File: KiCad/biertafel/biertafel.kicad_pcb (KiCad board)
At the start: 2 copper layers, 39 parts, among them J1 Screw_Terminal_01x02, J10 Screw_Terminal_01x02, J11 Raspberry connectors, J12 Screw_Terminal_01x02, J13 Raspberry connectors, J14 VCC socket, J2 Screw_Terminal_01x02, J3 Screw_Terminal_01x02, J4 Screw_Terminal_01x02, J5 Screw_Terminal_01x02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

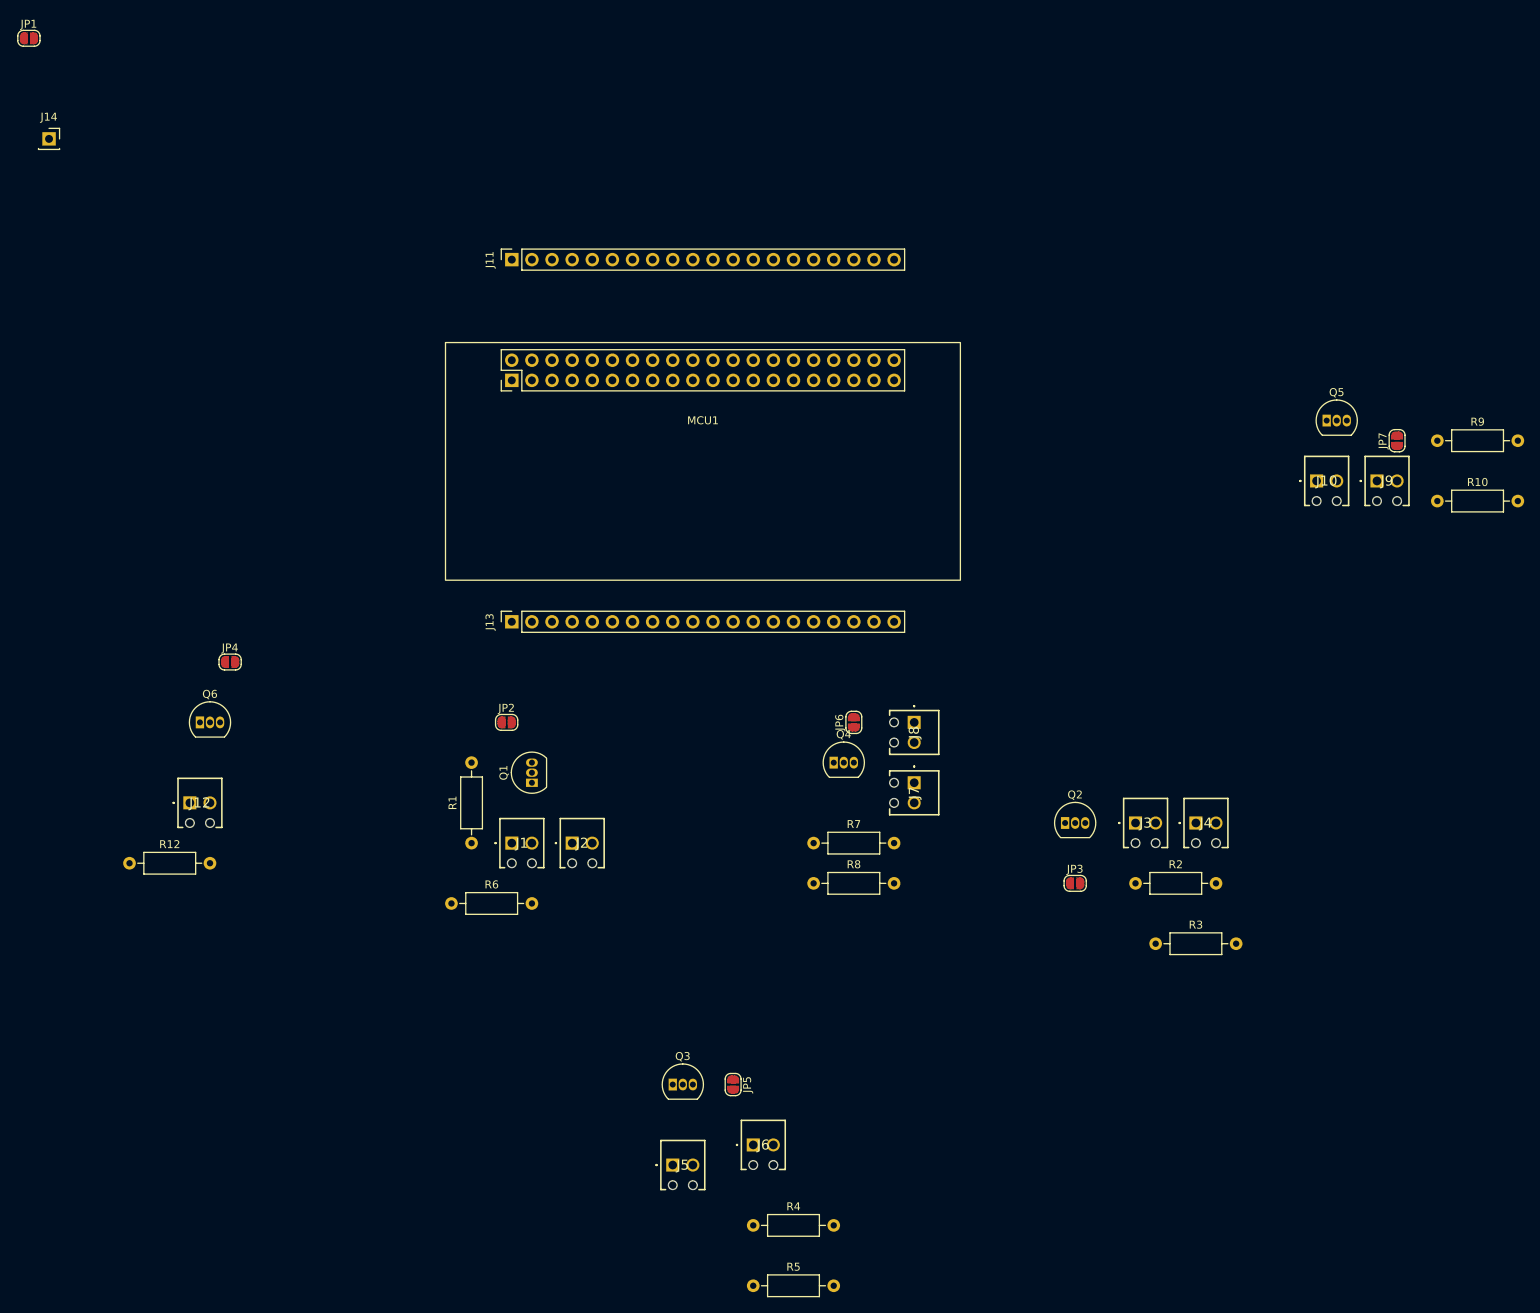
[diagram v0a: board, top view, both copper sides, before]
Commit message: In PCB layout, placed the objects to aprox position
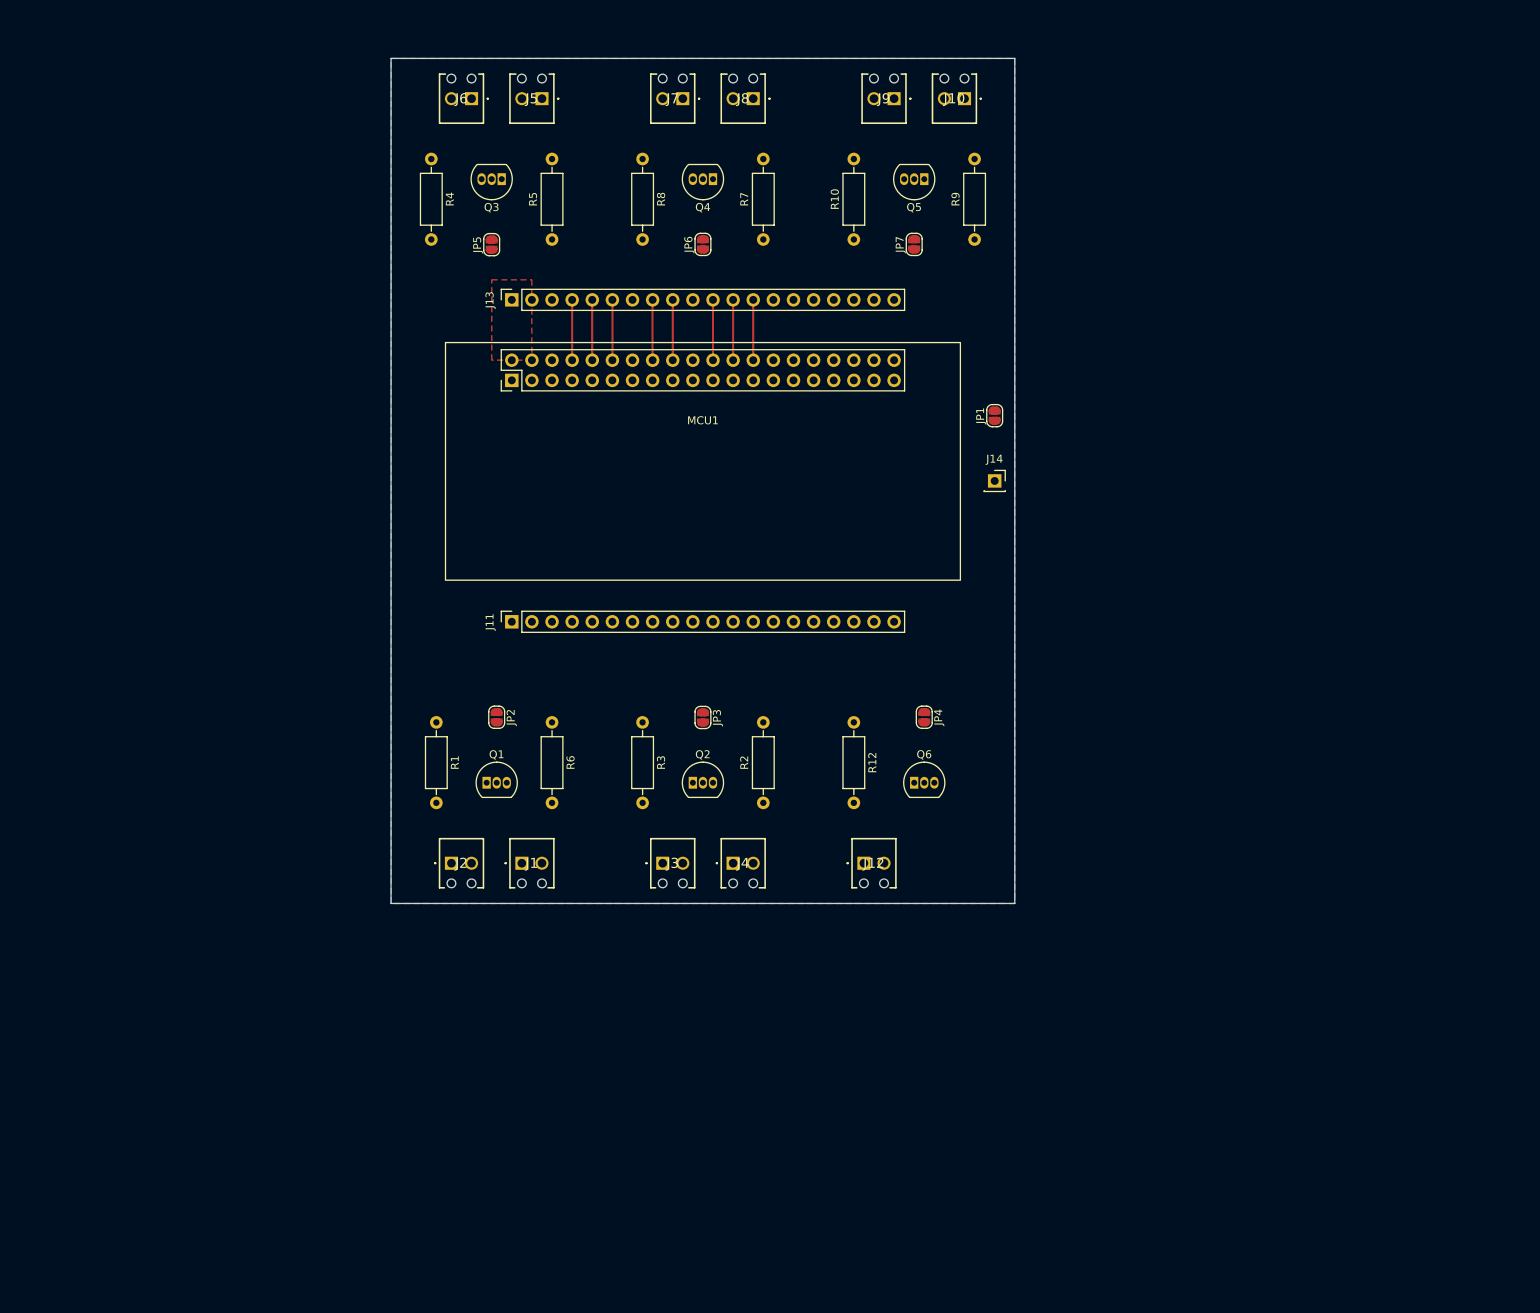
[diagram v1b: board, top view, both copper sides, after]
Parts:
- moved R4 140.6 mm to (109.2, 48.3), turned to -90 degrees
- moved J6 136.8 mm to (114.3, 40.6), turned to 180 degrees
- moved J5 135.6 mm to (123.2, 40.6), turned to 180 degrees
- moved R5 134.5 mm to (124.5, 58.4), turned to 90 degrees
- moved JP1 130.9 mm to (180.3, 80.7), turned to 90 degrees
- moved J14 126.9 mm to (180.3, 88.9)
- moved Q3 116.3 mm to (118.1, 50.8), turned to 180 degrees
- moved JP5 110.3 mm to (116.8, 59.1), turned to 90 degrees
- moved R8 94.0 mm to (135.9, 48.3), turned to -90 degrees
- moved R12 93.2 mm to (162.6, 119.4), turned to -90 degrees
- moved J7 91.2 mm to (141.0, 40.6), turned to 180 degrees
- moved Q6 90.5 mm to (170.2, 127.0)
- moved JP4 87.9 mm to (171.4, 118.7), turned to -90 degrees
- moved J12 85.4 mm to (163.8, 137.2)
- moved J8 81.3 mm to (149.9, 40.6), turned to 180 degrees
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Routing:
- net UART TX: track 0.00 -> 7.62 mm
- net UART RX: track 0.00 -> 7.62 mm
- net SPI CE1: track 0.00 -> 7.62 mm
- net SPI CE0: track 0.00 -> 7.62 mm
- net PWM GPIO18: track 0.00 -> 7.62 mm
- net LED3: track 0.00 -> 7.62 mm
- net BUTTON4: track 0.00 -> 7.62 mm
- net BUTTON3: track 0.00 -> 7.62 mm
- added copper zone on F.Cu, net +5V
- added copper zone on B.Cu, net GND
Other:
- board outline added: 78.7 x 106.7 mm

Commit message: PCB layout V0.1
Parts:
- moved J1 1.27 mm to (120.7, 135.9)
- moved J12 1.27 mm to (163.8, 135.9)
- moved J2 1.27 mm to (111.8, 135.9)
- moved J3 1.27 mm to (138.4, 135.9)
- moved J4 1.27 mm to (147.3, 135.9)
- moved JP2 1.27 mm to (117.5, 117.5)
- moved JP3 1.27 mm to (143.5, 117.5)
- moved JP4 1.27 mm to (171.4, 117.5)
- moved JP5 1.27 mm to (116.8, 60.3)
- moved JP6 1.27 mm to (143.5, 60.3)
- moved JP7 1.27 mm to (170.2, 60.3)
- moved Q3 1.27 mm to (118.1, 52.1)
- moved Q4 1.27 mm to (144.8, 52.1)
- moved Q5 1.27 mm to (171.4, 52.1)
- moved R4 1.27 mm to (109.2, 49.5)
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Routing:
- net +3V3: track 0.00 -> 285.3 mm
- net VCC: track 0.00 -> 273.1 mm
- net GND: track 0.00 -> 82.1 mm, vias 0 -> 4
- net BUTTON1: track 0.00 -> 64.4 mm
- net BUTTON2: track 0.00 -> 63.9 mm
- net LED2: track 0.00 -> 55.8 mm
- net LED1: track 0.00 -> 54.6 mm
- net BUZZER: track 0.00 -> 53.4 mm
- net BUTTON3: track 7.62 -> 58.8 mm
- net BUTTON5: track 0.00 -> 36.4 mm
- net BUTTON4: track 7.62 -> 38.7 mm
- net SPI SCLK: track 0.00 -> 30.5 mm
- net SPI MOSI: track 0.00 -> 30.5 mm
- net SPI MISO: track 0.00 -> 30.5 mm
- net PWM GPIO13: track 0.00 -> 30.5 mm
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- added copper zone on B.Cu, net +5V
- added copper zone on F.Cu, net GND
- added copper zone on F.Cu, net VCC
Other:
- board size 78.7 x 106.7 mm -> 78.7 x 105.4 mm
